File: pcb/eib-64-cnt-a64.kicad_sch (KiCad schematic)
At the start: 4 parts, among them J1 FOLC-110-01-S-Q, J2 FOLC-110-01-S-Q, J3 DF40C(2.0)-70DS-0.4V(51), J4 Conn_01x07_Male

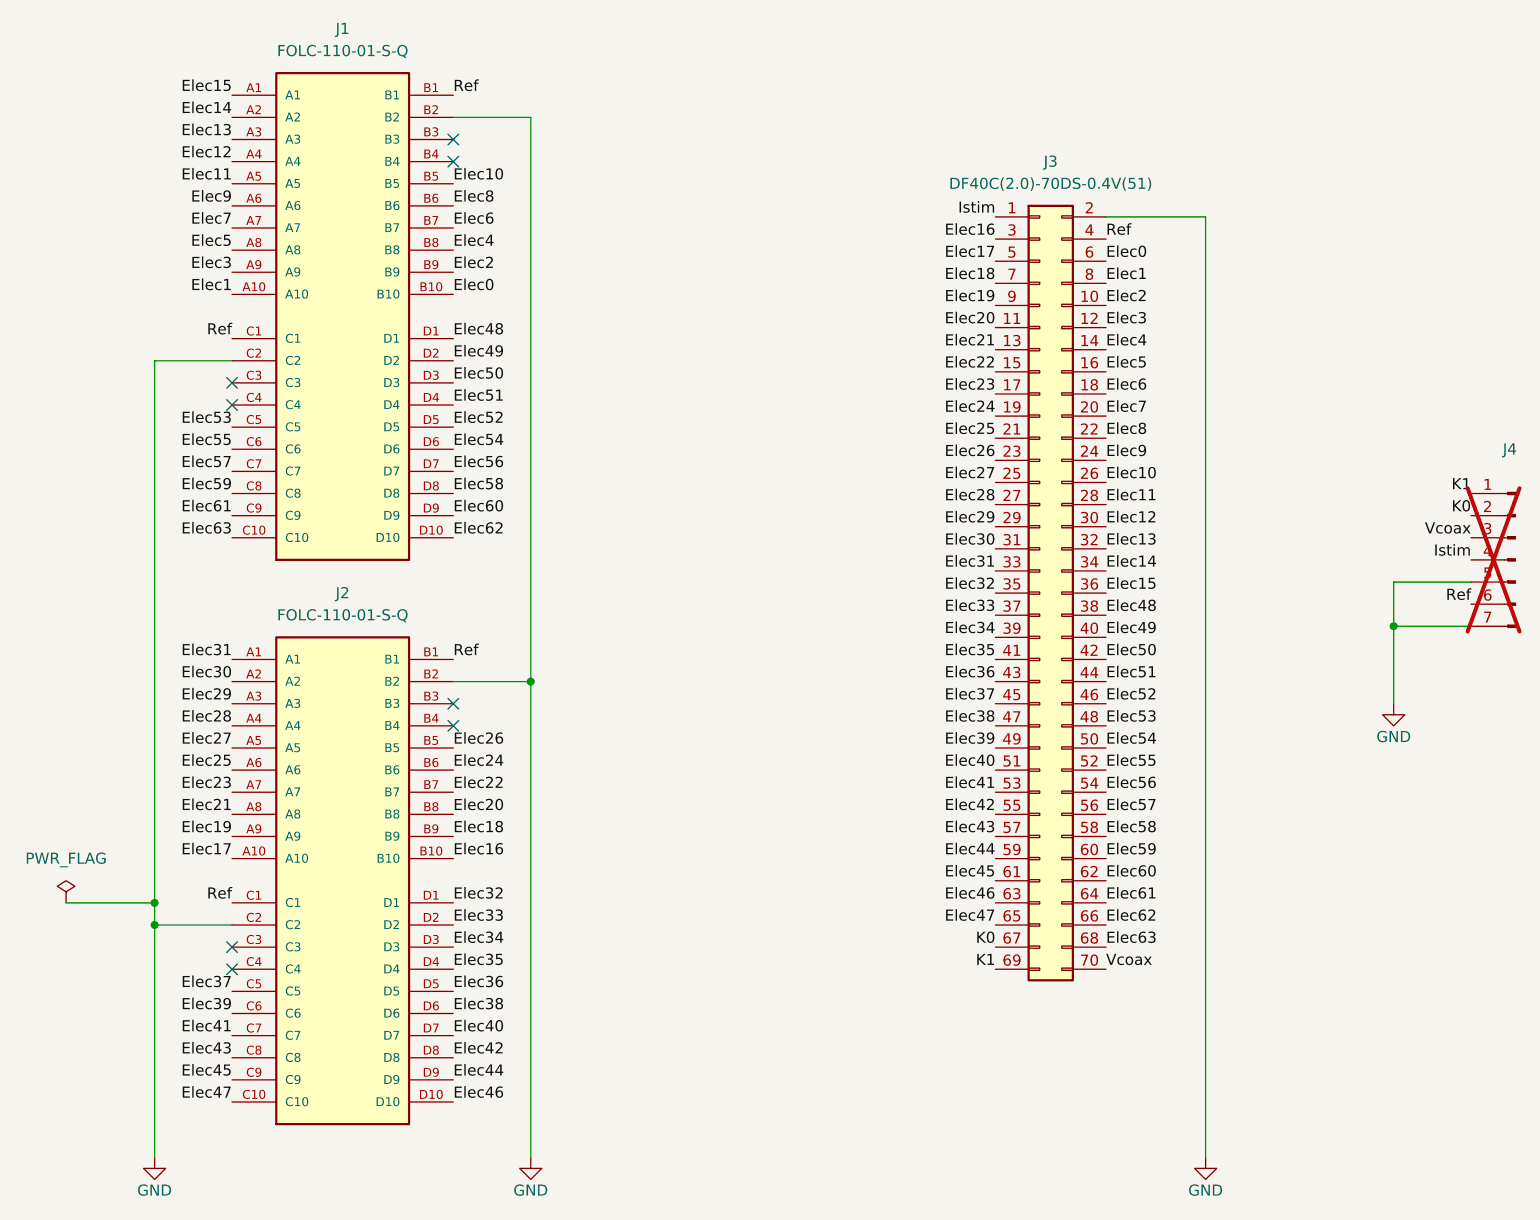
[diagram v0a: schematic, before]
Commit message: Revision A
- This was fabricated and tested.
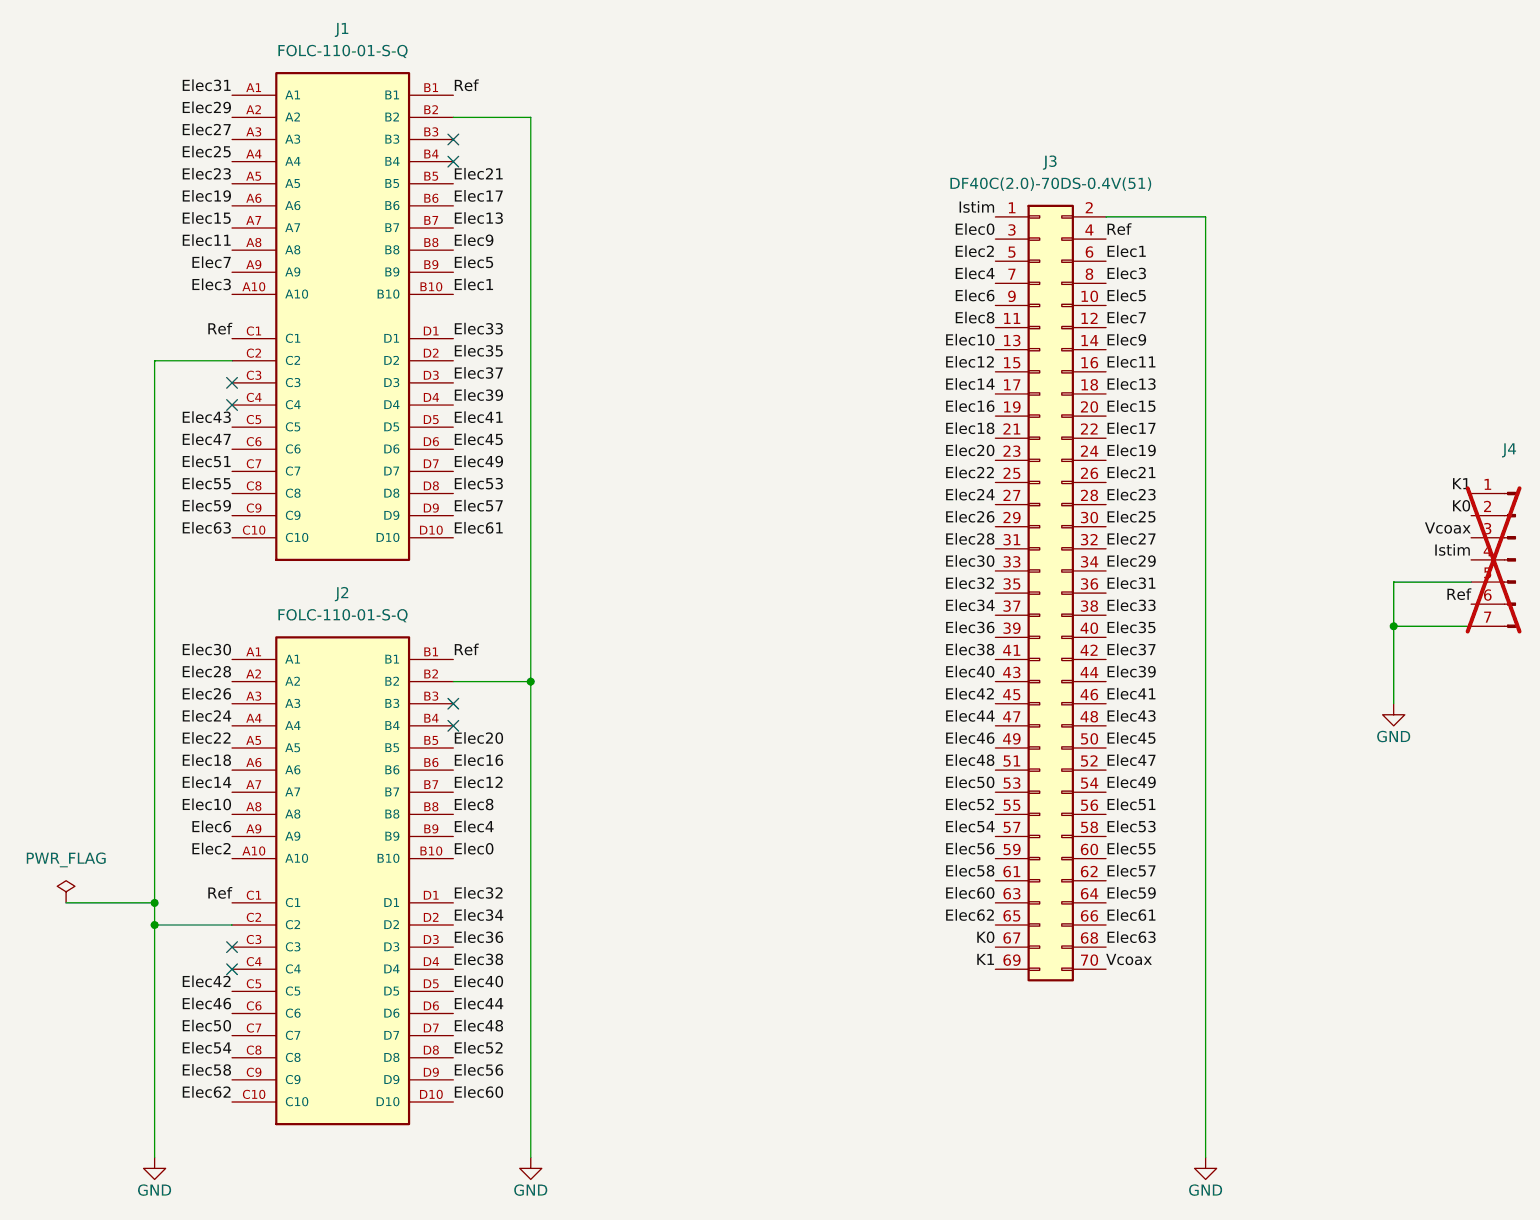
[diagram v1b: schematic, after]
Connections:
- net Elec0: now also J2.B10, J3.3 (Pin_3); no longer J1.B10, J3.6 (Pin_6)
- net Elec1: now also J1.B10, J3.6 (Pin_6); no longer J1.A10, J3.8 (Pin_8)
- net Elec10: now also J2.A8, J3.13 (Pin_13); no longer J1.B5, J3.26 (Pin_26)
- net Elec11: now also J1.A8, J3.16 (Pin_16); no longer J1.A5, J3.28 (Pin_28)
- net Elec12: now also J2.B7, J3.15 (Pin_15); no longer J1.A4, J3.30 (Pin_30)
- net Elec13: now also J1.B7, J3.18 (Pin_18); no longer J1.A3, J3.32 (Pin_32)
- net Elec14: now also J2.A7, J3.17 (Pin_17); no longer J1.A2, J3.34 (Pin_34)
- net Elec15: now also J1.A7, J3.20 (Pin_20); no longer J1.A1, J3.36 (Pin_36)
- net Elec16: now also J2.B6, J3.19 (Pin_19); no longer J2.B10, J3.3 (Pin_3)
- net Elec17: now also J1.B6, J3.22 (Pin_22); no longer J2.A10, J3.5 (Pin_5)
- net Elec18: now also J2.A6, J3.21 (Pin_21); no longer J2.B9, J3.7 (Pin_7)
- net Elec19: now also J1.A6, J3.24 (Pin_24); no longer J2.A9, J3.9 (Pin_9)
- net Elec2: now also J2.A10, J3.5 (Pin_5); no longer J1.B9, J3.10 (Pin_10)
- net Elec20: now also J2.B5, J3.23 (Pin_23); no longer J2.B8, J3.11 (Pin_11)
- net Elec21: now also J1.B5, J3.26 (Pin_26); no longer J2.A8, J3.13 (Pin_13)
- net Elec22: now also J2.A5, J3.25 (Pin_25); no longer J2.B7, J3.15 (Pin_15)
- net Elec23: now also J1.A5, J3.28 (Pin_28); no longer J2.A7, J3.17 (Pin_17)
- net Elec24: now also J2.A4, J3.27 (Pin_27); no longer J2.B6, J3.19 (Pin_19)
- net Elec25: now also J1.A4, J3.30 (Pin_30); no longer J2.A6, J3.21 (Pin_21)
- net Elec26: now also J2.A3, J3.29 (Pin_29); no longer J2.B5, J3.23 (Pin_23)
- net Elec27: now also J1.A3, J3.32 (Pin_32); no longer J2.A5, J3.25 (Pin_25)
- net Elec28: now also J2.A2, J3.31 (Pin_31); no longer J2.A4, J3.27 (Pin_27)
- net Elec29: now also J1.A2, J3.34 (Pin_34); no longer J2.A3, J3.29 (Pin_29)
- net Elec3: now also J1.A10, J3.8 (Pin_8); no longer J1.A9, J3.12 (Pin_12)
- net Elec30: now also J2.A1, J3.33 (Pin_33); no longer J2.A2, J3.31 (Pin_31)
- net Elec31: now also J1.A1, J3.36 (Pin_36); no longer J2.A1, J3.33 (Pin_33)
- net Elec33: now also J1.D1, J3.38 (Pin_38); no longer J2.D2, J3.37 (Pin_37)
- net Elec34: now also J2.D2, J3.37 (Pin_37); no longer J2.D3, J3.39 (Pin_39)
- net Elec35: now also J1.D2, J3.40 (Pin_40); no longer J2.D4, J3.41 (Pin_41)
- net Elec36: now also J2.D3, J3.39 (Pin_39); no longer J2.D5, J3.43 (Pin_43)
- net Elec37: now also J1.D3, J3.42 (Pin_42); no longer J2.C5, J3.45 (Pin_45)
- net Elec38: now also J2.D4, J3.41 (Pin_41); no longer J2.D6, J3.47 (Pin_47)
- net Elec39: now also J1.D4, J3.44 (Pin_44); no longer J2.C6, J3.49 (Pin_49)
- net Elec4: now also J2.B9, J3.7 (Pin_7); no longer J1.B8, J3.14 (Pin_14)
- net Elec40: now also J2.D5, J3.43 (Pin_43); no longer J2.D7, J3.51 (Pin_51)
- net Elec41: now also J1.D5, J3.46 (Pin_46); no longer J2.C7, J3.53 (Pin_53)
- net Elec42: now also J2.C5, J3.45 (Pin_45); no longer J2.D8, J3.55 (Pin_55)
- net Elec43: now also J1.C5, J3.48 (Pin_48); no longer J2.C8, J3.57 (Pin_57)
- net Elec44: now also J2.D6, J3.47 (Pin_47); no longer J2.D9, J3.59 (Pin_59)
- net Elec45: now also J1.D6, J3.50 (Pin_50); no longer J2.C9, J3.61 (Pin_61)
- net Elec46: now also J2.C6, J3.49 (Pin_49); no longer J2.D10, J3.63 (Pin_63)
- net Elec47: now also J1.C6, J3.52 (Pin_52); no longer J2.C10, J3.65 (Pin_65)
- net Elec48: now also J2.D7, J3.51 (Pin_51); no longer J1.D1, J3.38 (Pin_38)
- net Elec49: now also J1.D7, J3.54 (Pin_54); no longer J1.D2, J3.40 (Pin_40)
- net Elec5: now also J1.B9, J3.10 (Pin_10); no longer J1.A8, J3.16 (Pin_16)
- net Elec50: now also J2.C7, J3.53 (Pin_53); no longer J1.D3, J3.42 (Pin_42)
- net Elec51: now also J1.C7, J3.56 (Pin_56); no longer J1.D4, J3.44 (Pin_44)
- net Elec52: now also J2.D8, J3.55 (Pin_55); no longer J1.D5, J3.46 (Pin_46)
- net Elec53: now also J1.D8, J3.58 (Pin_58); no longer J1.C5, J3.48 (Pin_48)
- net Elec54: now also J2.C8, J3.57 (Pin_57); no longer J1.D6, J3.50 (Pin_50)
- net Elec55: now also J1.C8, J3.60 (Pin_60); no longer J1.C6, J3.52 (Pin_52)
- net Elec56: now also J2.D9, J3.59 (Pin_59); no longer J1.D7, J3.54 (Pin_54)
- net Elec57: now also J1.D9, J3.62 (Pin_62); no longer J1.C7, J3.56 (Pin_56)
- net Elec58: now also J2.C9, J3.61 (Pin_61); no longer J1.D8, J3.58 (Pin_58)
- net Elec59: now also J1.C9, J3.64 (Pin_64); no longer J1.C8, J3.60 (Pin_60)
- net Elec6: now also J2.A9, J3.9 (Pin_9); no longer J1.B7, J3.18 (Pin_18)
- net Elec60: now also J2.D10, J3.63 (Pin_63); no longer J1.D9, J3.62 (Pin_62)
- net Elec61: now also J1.D10, J3.66 (Pin_66); no longer J1.C9, J3.64 (Pin_64)
- net Elec62: now also J2.C10, J3.65 (Pin_65); no longer J1.D10, J3.66 (Pin_66)
- net Elec7: now also J1.A9, J3.12 (Pin_12); no longer J1.A7, J3.20 (Pin_20)
- net Elec8: now also J2.B8, J3.11 (Pin_11); no longer J1.B6, J3.22 (Pin_22)
- net Elec9: now also J1.B8, J3.14 (Pin_14); no longer J1.A6, J3.24 (Pin_24)
